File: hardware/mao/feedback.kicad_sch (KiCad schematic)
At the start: 22 parts, among them J501 LRA, Q501 AO3400A, U501 MAX98357AETE+T, U502 DRV2605LDGSR, U503 IRM-H638T/TR2, U504 TPS22916CYFPR

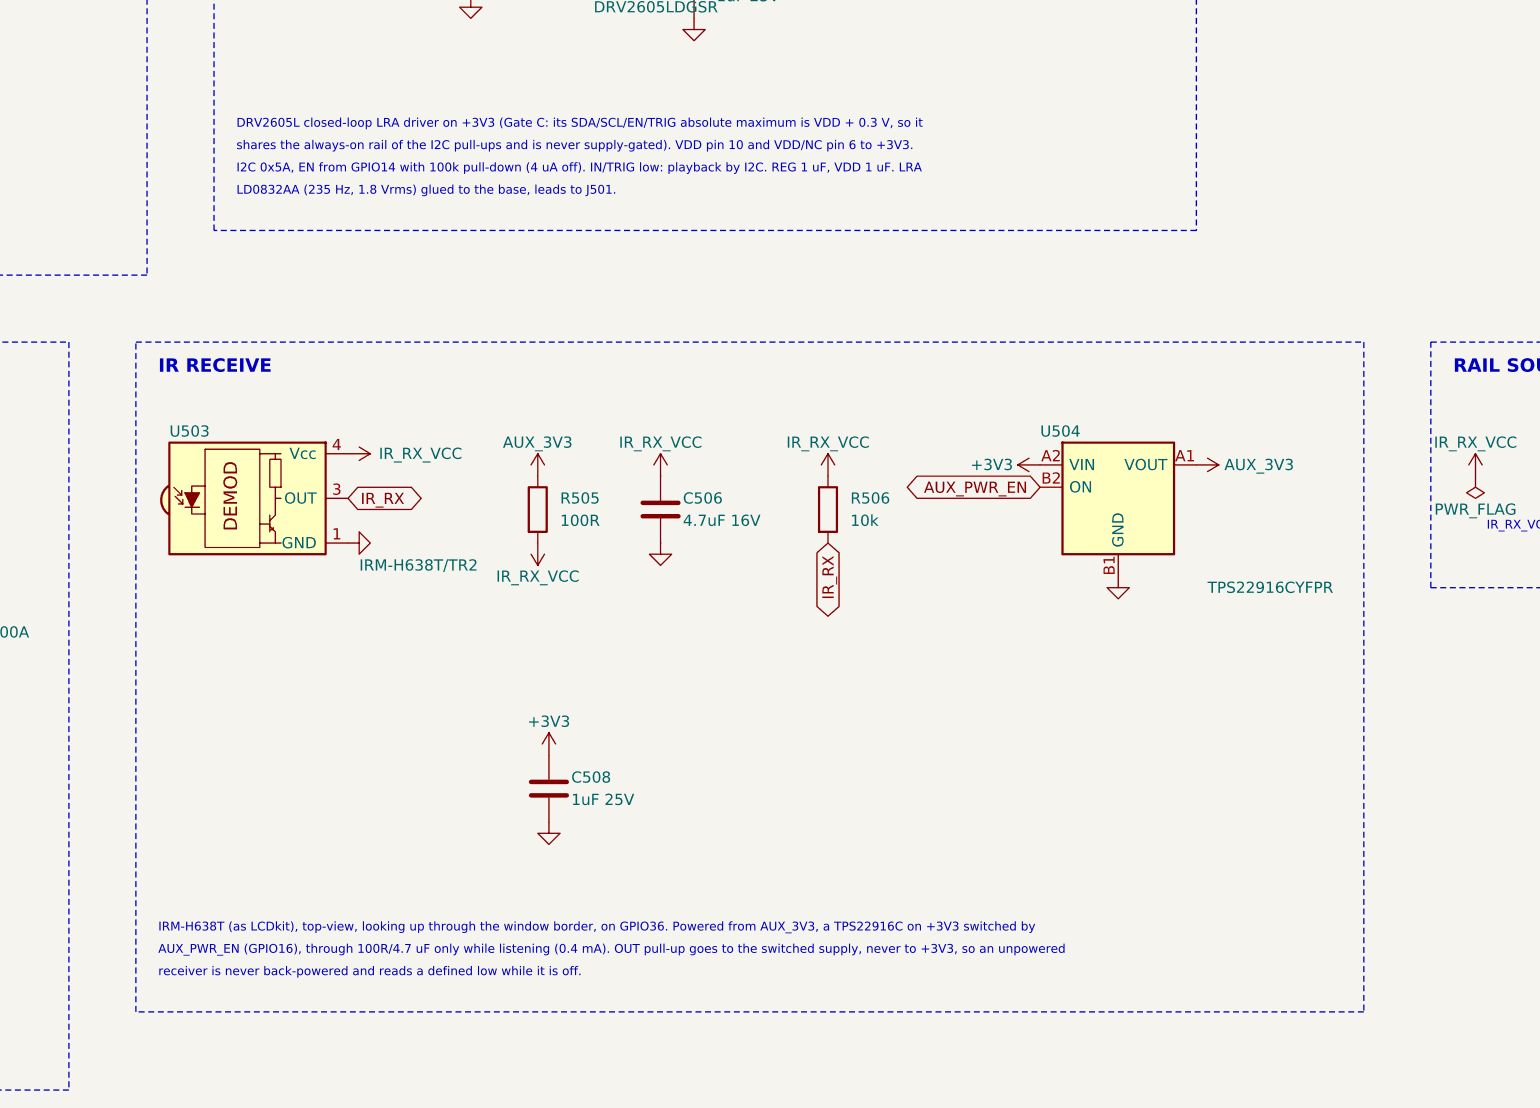
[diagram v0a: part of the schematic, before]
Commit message: A1 capture/layout follow the pin swaps (ERC 0); escapes and fixture pads moved with their nets
Co-Authored-By: Claude Opus 5.5 <noreply@anthropic.com>
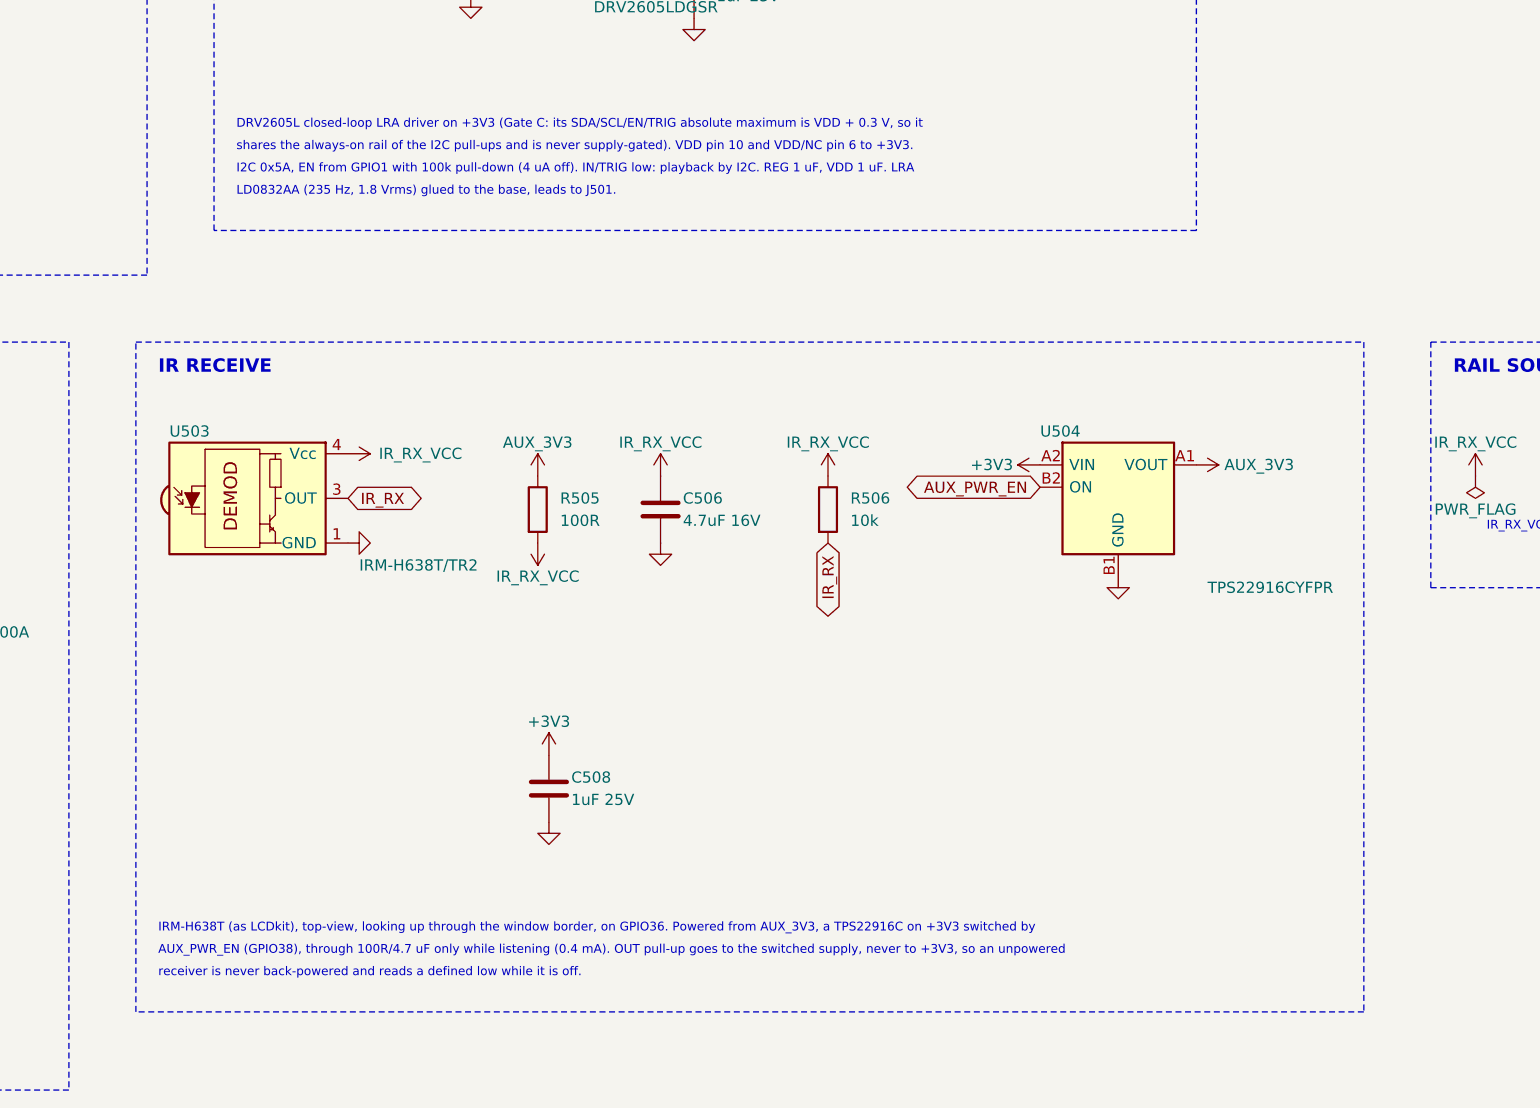
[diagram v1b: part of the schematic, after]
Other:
- note added: "AUX_PWR_EN (GPIO38), through 100R/4.7 uF only while listening (0.4 mA). OUT pull-up goes to the switched supply, never to +3V3, so an unpowered"
- note added: "I2C 0x5A, EN from GPIO1 with 100k pull-down (4 uA off). IN/TRIG low: playback by I2C. REG 1 uF, VDD 1 uF. LRA"
- note removed: "AUX_PWR_EN (GPIO16), through 100R/4.7 uF only while listening (0.4 mA). OUT pull-up goes to the switched supply, never to +3V3, so an unpowered"
- note removed: "I2C 0x5A, EN from GPIO14 with 100k pull-down (4 uA off). IN/TRIG low: playback by I2C. REG 1 uF, VDD 1 uF. LRA"
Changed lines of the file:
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@@
 		)
 	)
-	(text "I2C 0x5A, EN from GPIO14 with 100k pull-down (4 uA off). IN/TRIG low: playback by I2C. REG 1 uF, VDD 1 uF. LRA"
+	(text "I2C 0x5A, EN from GPIO1 with 100k pull-down (4 uA off). IN/TRIG low: playback by I2C. REG 1 uF, VDD 1 uF. LRA"
 		(exclude_from_sim no)
 		(at 163.83 77.47 0)
@@
 		)
 	)
-	(text "AUX_PWR_EN (GPIO16), through 100R/4.7 uF only while listening (0.4 mA). OUT pull-up goes to the switched supply, never to +3V3, so an unpowered"
+	(text "AUX_PWR_EN (GPIO38), through 100R/4.7 uF only while listening (0.4 mA). OUT pull-up goes to the switched supply, never to +3V3, so an unpowered"
 		(exclude_from_sim no)
 		(at 154.94 166.37 0)

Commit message: A1 BOM (design review 2026-10-06): charger IN/BAT 2.2 uF 25 V 0402, DRV2605LDGST, DMG2302UKQ-7; backlight reference 95.8 mV -> 29.0 mA
C101/C103 move from 1 uF to 2.2 uF 25 V 0402 (CL05A225KA5NUNC, C307418) so at least 1 uF remains under DC bias
(TI SLUSF65B 7.2.2.3). DRV2605LDGSR -> DRV2605LDGST (C425927, same part, 250 reel) and DMG2302UK-7 -> DMG2302UKQ-7
(C5224573, same pinout) for stock. Fixes the backlight arithmetic in the capture notes (N7).

Co-Authored-By: Claude Opus 5.5 <noreply@anthropic.com>
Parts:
- U502: value DRV2605LDGSR -> DRV2605LDGST; LCSC C527464 -> C425927; MPN DRV2605LDGSR -> DRV2605LDGST
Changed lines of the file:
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@@
 			)
 		)
-		(property "Value" "DRV2605LDGSR"
+		(property "Value" "DRV2605LDGST"
 			(at 204.47 58.42 0)
 			(effects
@@
 			)
 		)
-		(property "Description" "haptic driver, auto-resonance"
+		(property "Description" "haptic driver, auto-resonance (DGST: the DGSR part on a 250-piece reel)"
 			(at 190.5 46.99 0)
 			(effects
@@
 			)
 		)
-		(property "MPN" "DRV2605LDGSR"
+		(property "MPN" "DRV2605LDGST"
 			(at 190.5 46.99 0)
 			(effects
@@
 			)
 		)
-		(property "LCSC" "C527464"
+		(property "LCSC" "C425927"
 			(at 190.5 46.99 0)
 			(effects
